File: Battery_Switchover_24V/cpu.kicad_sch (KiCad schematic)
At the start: 39 parts, among them J1 USB_C_Receptacle_USB2.0_14P, M1 Fan, Q1 PZT2222AT1G, SW1 SW_Push, U14 OPA2197xD, U3 LPC11U14FBD48-201, Y1 12.000MHz

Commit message: adding BMS and changed topology
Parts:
- D3: footprint Diode_THT:D_5W_P10.16mm_Horizontal -> Diode_SMD:D_SMA_Handsoldering
- M1: footprint Connector_PinHeader_2.54mm:PinHeader_1x02_P2.54mm_Vertical -> TerminalBlock_Phoenix:TerminalBlock_Phoenix_PT-1,5-2-3.5-H_1x02_P3.50mm_Horizontal
- Y1: footprint Crystal:Crystal_SMD_HC49-SD -> Crystal:Crystal_SMD_TXC_7M-4Pin_3.2x2.5mm
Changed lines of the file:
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@@
 			)
 		)
-		(property "Footprint" "Diode_THT:D_5W_P10.16mm_Horizontal"
+		(property "Footprint" "Diode_SMD:D_SMA_Handsoldering"
 			(at 248.92 120.65 0)
 			(effects
@@
 			)
 		)
-		(property "Footprint" "Crystal:Crystal_SMD_HC49-SD"
+		(property "Footprint" "Crystal:Crystal_SMD_TXC_7M-4Pin_3.2x2.5mm"
 			(at 148.59 107.95 0)
 			(effects
@@
 			)
 		)
-		(property "Footprint" "Connector_PinHeader_2.54mm:PinHeader_1x02_P2.54mm_Vertical"
+		(property "Footprint" "TerminalBlock_Phoenix:TerminalBlock_Phoenix_PT-1,5-2-3.5-H_1x02_P3.50mm_Horizontal"
 			(at 256.54 121.666 0)
 			(effects

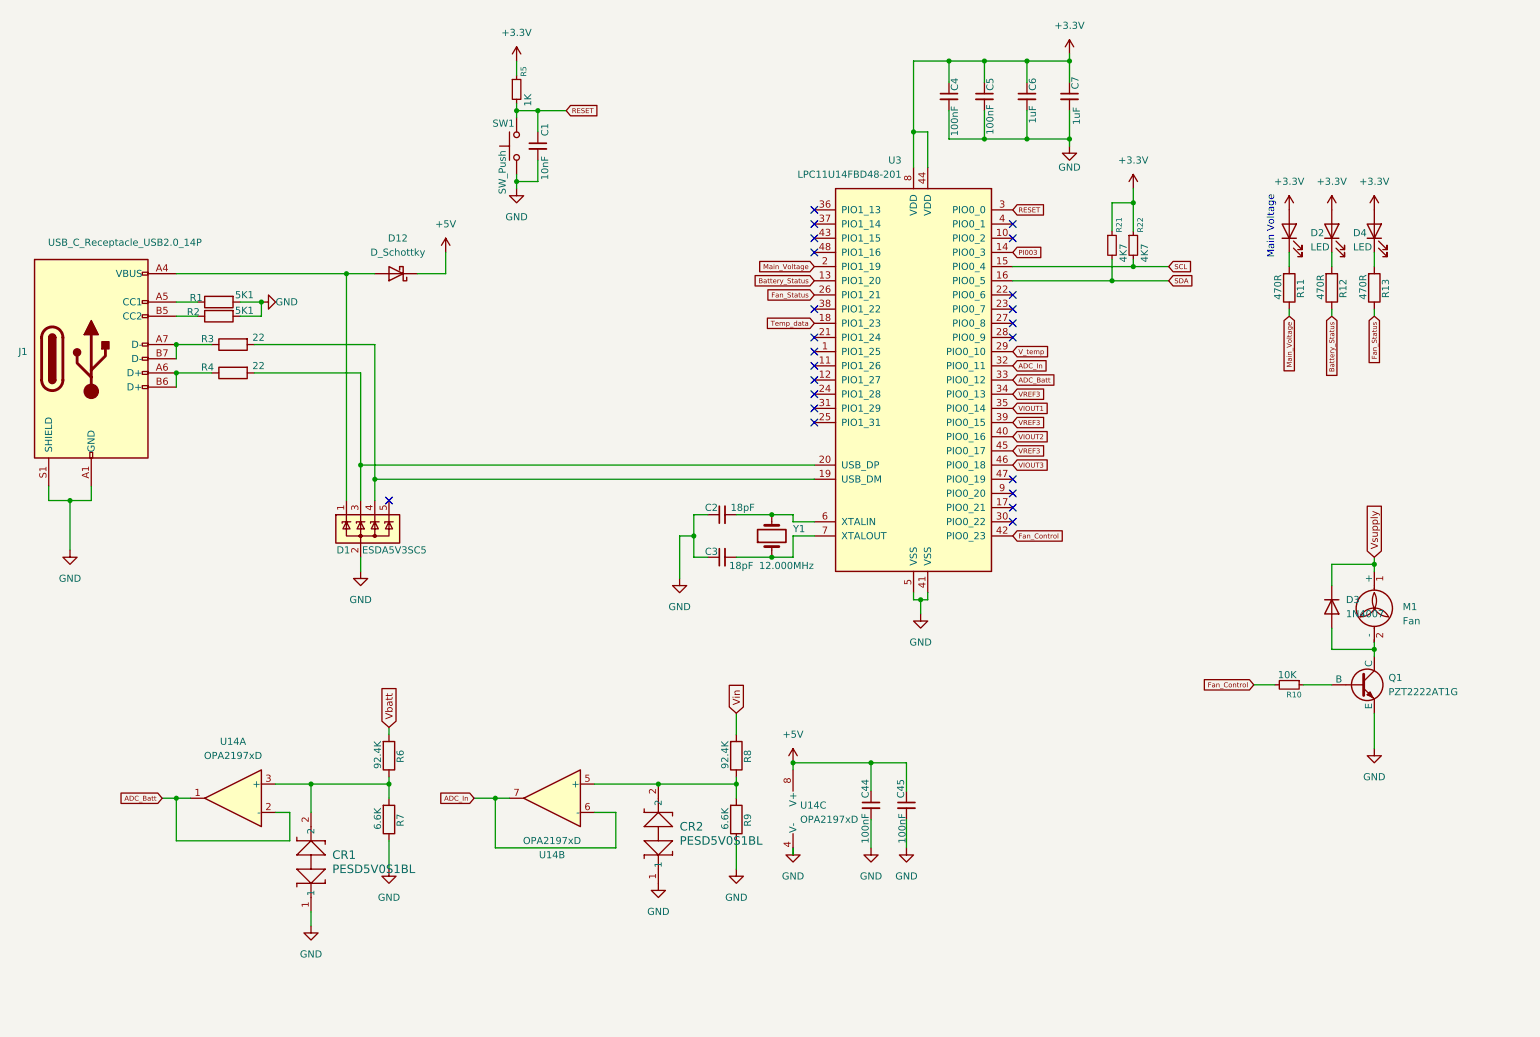
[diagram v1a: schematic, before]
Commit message: Changed current sensor (fewer analog pins), added extra adc
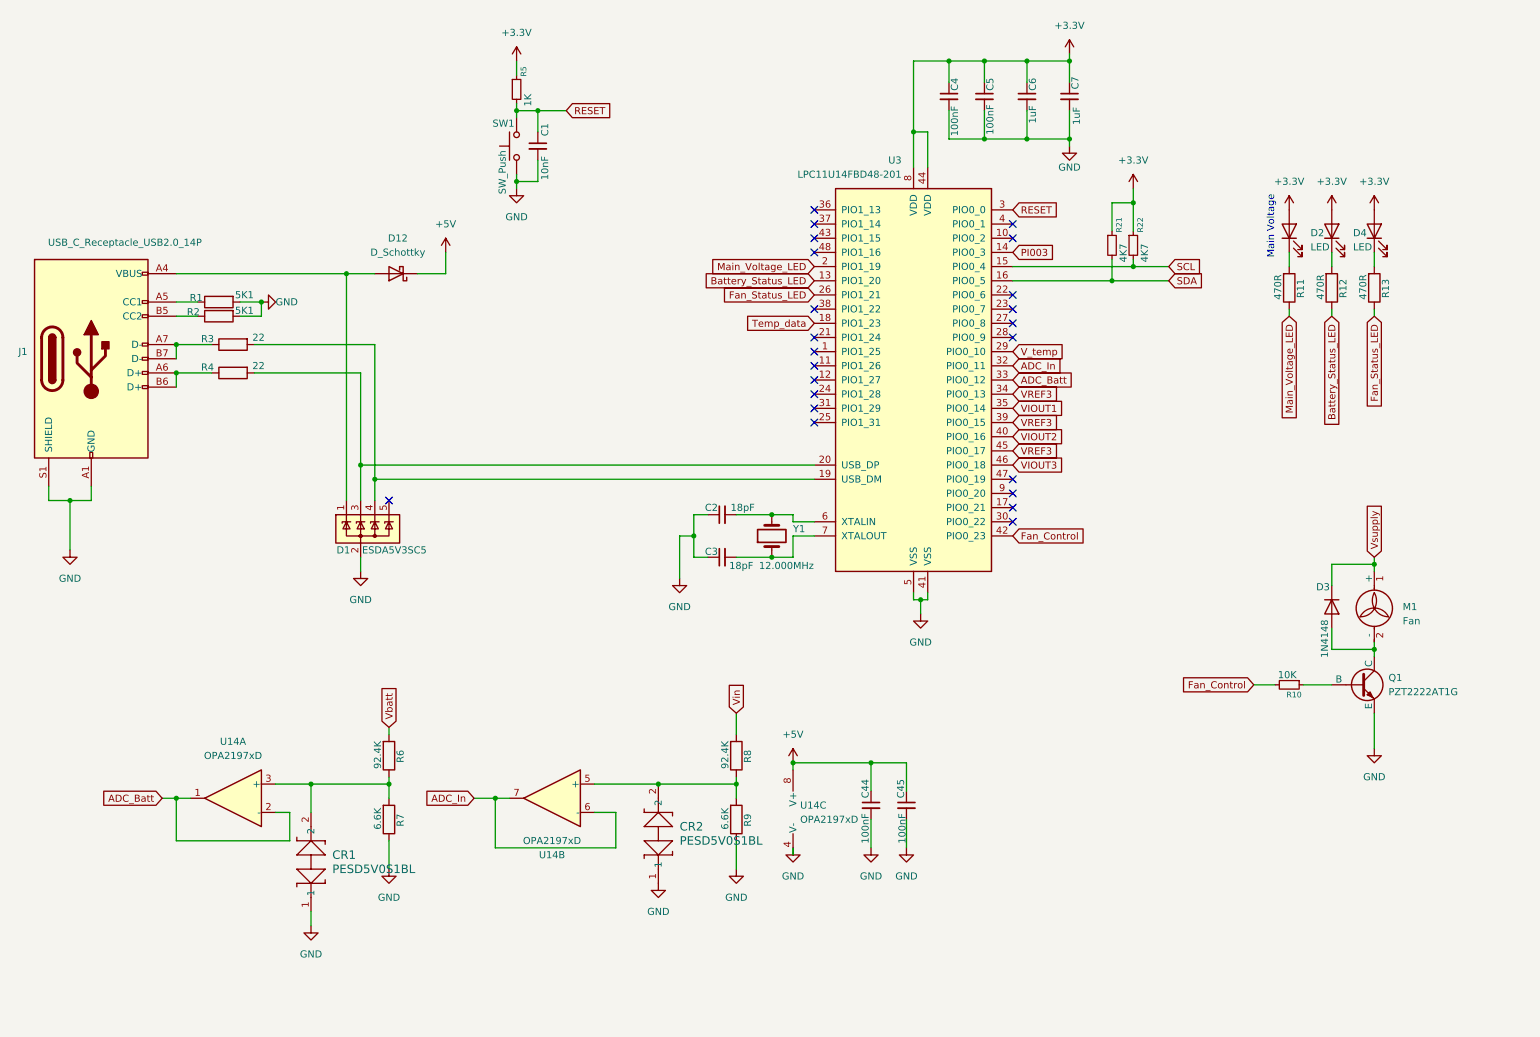
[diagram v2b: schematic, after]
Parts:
- D3: value 1N4007 -> 1N4148
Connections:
- net Battery_Status renamed Battery_Status_LED
- net Fan_Status renamed Fan_Status_LED
- net Main_Voltage renamed Main_Voltage_LED
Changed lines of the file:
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@@
 		)
 	)
-	(global_label "Fan_Status"
+	(global_label "Fan_Status_LED"
 		(shape input)
 		(at 156.21 64.77 180)
@@
 		(effects
 			(font
-				(size 0.889 0.889)
+				(size 1.27 1.27)
 			)
 			(justify right)
 		)
 		(property "Intersheetrefs" "${INTERSHEET_REFS}"
-			(at 146.8816 64.77 0)
+			(at 138.4689 64.77 0)
 			(effects
 				(font
@@
 		(effects
 			(font
-				(size 0.889 0.889)
+				(size 1.27 1.27)
 			)
 			(justify left)
@@
 		)
 	)
-	(global_label "Main_Voltage"
+	(global_label "Main_Voltage_LED"
 		(shape input)
 		(at 156.21 59.69 180)
@@
 		(effects
 			(font
-				(size 0.889 0.889)
+				(size 1.27 1.27)
 			)
 			(justify right)
 		)
 		(property "Intersheetrefs" "${INTERSHEET_REFS}"
-			(at 145.4847 59.69 0)
+			(at 136.4732 59.69 0)
 			(effects
 				(font
@@
 		(effects
 			(font
-				(size 0.889 0.889)
+				(size 1.27 1.27)
 			)
 			(justify left)
@@
 		)
 	)
-	(global_label "Battery_Status"
+	(global_label "Battery_Status_LED"
 		(shape input)
 		(at 156.21 62.23 180)
@@
 		(effects
 			(font
-				(size 0.889 0.889)
+				(size 1.27 1.27)
 			)
 			(justify right)
 		)
 		(property "Intersheetrefs" "${INTERSHEET_REFS}"
-			(at 144.5533 62.23 0)
+			(at 135.1427 62.23 0)
 			(effects
 				(font
@@
 		(effects
 			(font
-				(size 0.889 0.889)
-			)
-			(justify left)
-		)
-		(property "Intersheetrefs" "${INTERSHEET_REFS}"
-			(at 197.8811 49.53 0)
+				(size 1.27 1.27)
+			)
+			(justify left)
+		)
+		(property "Intersheetrefs" "${INTERSHEET_REFS}"
+			(at 200.5003 49.53 0)
 			(effects
 				(font
@@
 		(effects
 			(font
-				(size 0.889 0.889)
-			)
-			(justify left)
-		)
-		(property "Intersheetrefs" "${INTERSHEET_REFS}"
-			(at 224.2972 62.23 0)
+				(size 1.27 1.27)
+			)
+			(justify left)
+		)
+		(property "Intersheetrefs" "${INTERSHEET_REFS}"
+			(at 226.2633 62.23 0)
 			(effects
 				(font
@@
 		(effects
 			(font
-				(size 0.889 0.889)
+				(size 1.27 1.27)
 			)
 			(justify left)
@@
 		(effects
 			(font
-				(size 0.889 0.889)
-			)
-			(justify left)
-		)
-		(property "Intersheetrefs" "${INTERSHEET_REFS}"
-			(at 224.2549 59.69 0)
+				(size 1.27 1.27)
+			)
+			(justify left)
+		)
+		(property "Intersheetrefs" "${INTERSHEET_REFS}"
+			(at 226.2028 59.69 0)
 			(effects
 				(font
@@
 		(effects
 			(font
-				(size 0.889 0.889)
+				(size 1.27 1.27)
 			)
 			(justify left)
@@
 		(effects
 			(font
-				(size 0.889 0.889)
+				(size 1.27 1.27)
 			)
 			(justify left)
@@
 		(effects
 			(font
-				(size 0.889 0.889)
+				(size 1.27 1.27)
 			)
 			(justify right)
@@
 		(effects
 			(font
-				(size 0.889 0.889)
+				(size 1.27 1.27)
 			)
 			(justify left)
@@
 		(effects
 			(font
-				(size 0.889 0.889)
+				(size 1.27 1.27)
 			)
 			(justify right)
@@
 		(effects
 			(font
-				(size 0.889 0.889)
-			)
-			(justify left)
-		)
-		(property "Intersheetrefs" "${INTERSHEET_REFS}"
-			(at 197.7119 57.15 0)
+				(size 1.27 1.27)
+			)
+			(justify left)
+		)
+		(property "Intersheetrefs" "${INTERSHEET_REFS}"
+			(at 200.2585 57.15 0)
 			(effects
 				(font
@@
 		(effects
 			(font
-				(size 0.889 0.889)
+				(size 1.27 1.27)
 			)
 			(justify right)
 		)
 		(property "Intersheetrefs" "${INTERSHEET_REFS}"
-			(at 147.0934 69.85 0)
+			(at 143.186 69.85 0)
 			(effects
 				(font
@@
 		(effects
 			(font
-				(size 0.889 0.889)
+				(size 1.27 1.27)
 			)
 			(justify left)
@@
 		)
 	)
-	(global_label "Main_Voltage"
+	(global_label "Main_Voltage_LED"
 		(shape input)
 		(at 241.3 68.58 270)
@@
 		(effects
 			(font
-				(size 0.889 0.889)
+				(size 1.27 1.27)
 			)
 			(justify right)
 		)
 		(property "Intersheetrefs" "${INTERSHEET_REFS}"
-			(at 241.3 79.3053 90)
+			(at 241.3 82.3956 90)
 			(effects
 				(font
@@
 		)
 	)
-	(global_label "Battery_Status"
+	(global_label "Battery_Status_LED"
 		(shape input)
 		(at 248.92 68.58 270)
@@
 		(effects
 			(font
-				(size 0.889 0.889)
+				(size 1.27 1.27)
 			)
 			(justify right)
 		)
 		(property "Intersheetrefs" "${INTERSHEET_REFS}"
-			(at 248.92 80.2367 90)
+			(at 248.92 83.327 90)
 			(effects
 				(font
@@
 		(effects
 			(font
-				(size 0.889 0.889)
+				(size 1.27 1.27)
 			)
 			(justify left)
@@
 		)
 	)
-	(global_label "Fan_Status"
+	(global_label "Fan_Status_LED"
 		(shape input)
 		(at 256.54 68.58 270)
@@
 		(effects
 			(font
-				(size 0.889 0.889)
+				(size 1.27 1.27)
 			)
 			(justify right)
 		)
 		(property "Intersheetrefs" "${INTERSHEET_REFS}"
-			(at 256.54 77.9084 90)
+			(at 256.54 80.9987 90)
 			(effects
 				(font
@@
 		(effects
 			(font
-				(size 0.889 0.889)
+				(size 1.27 1.27)
 			)
 			(justify right)
@@
 		(effects
 			(font
-				(size 0.889 0.889)
+				(size 1.27 1.27)
 			)
 			(justify left)
@@
 		(effects
 			(font
-				(size 0.889 0.889)
+				(size 1.27 1.27)
 			)
 			(justify left)
@@
 		(effects
 			(font
-				(size 0.889 0.889)
+				(size 1.27 1.27)
 			)
 			(justify left)
@@
 		(on_board yes)
 		(dnp no)
-		(fields_autoplaced yes)
 		(property "Reference" "D3"
-			(at 251.46 119.3799 90)
-			(effects
-				(font
-					(size 1.27 1.27)
-				)
-				(justify left)
-			)
-		)
-		(property "Value" "1N4007"
-			(at 251.46 121.9199 90)
-			(effects
-				(font
+			(at 246.126 117.094 90)
+			(effects
+				(font
+					(size 1.27 1.27)
+				)
+				(justify left)
+			)
+		)
+		(property "Value" "1N4148"
+			(at 247.65 122.936 0)
+			(effects
+				(font

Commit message: Labels assigned
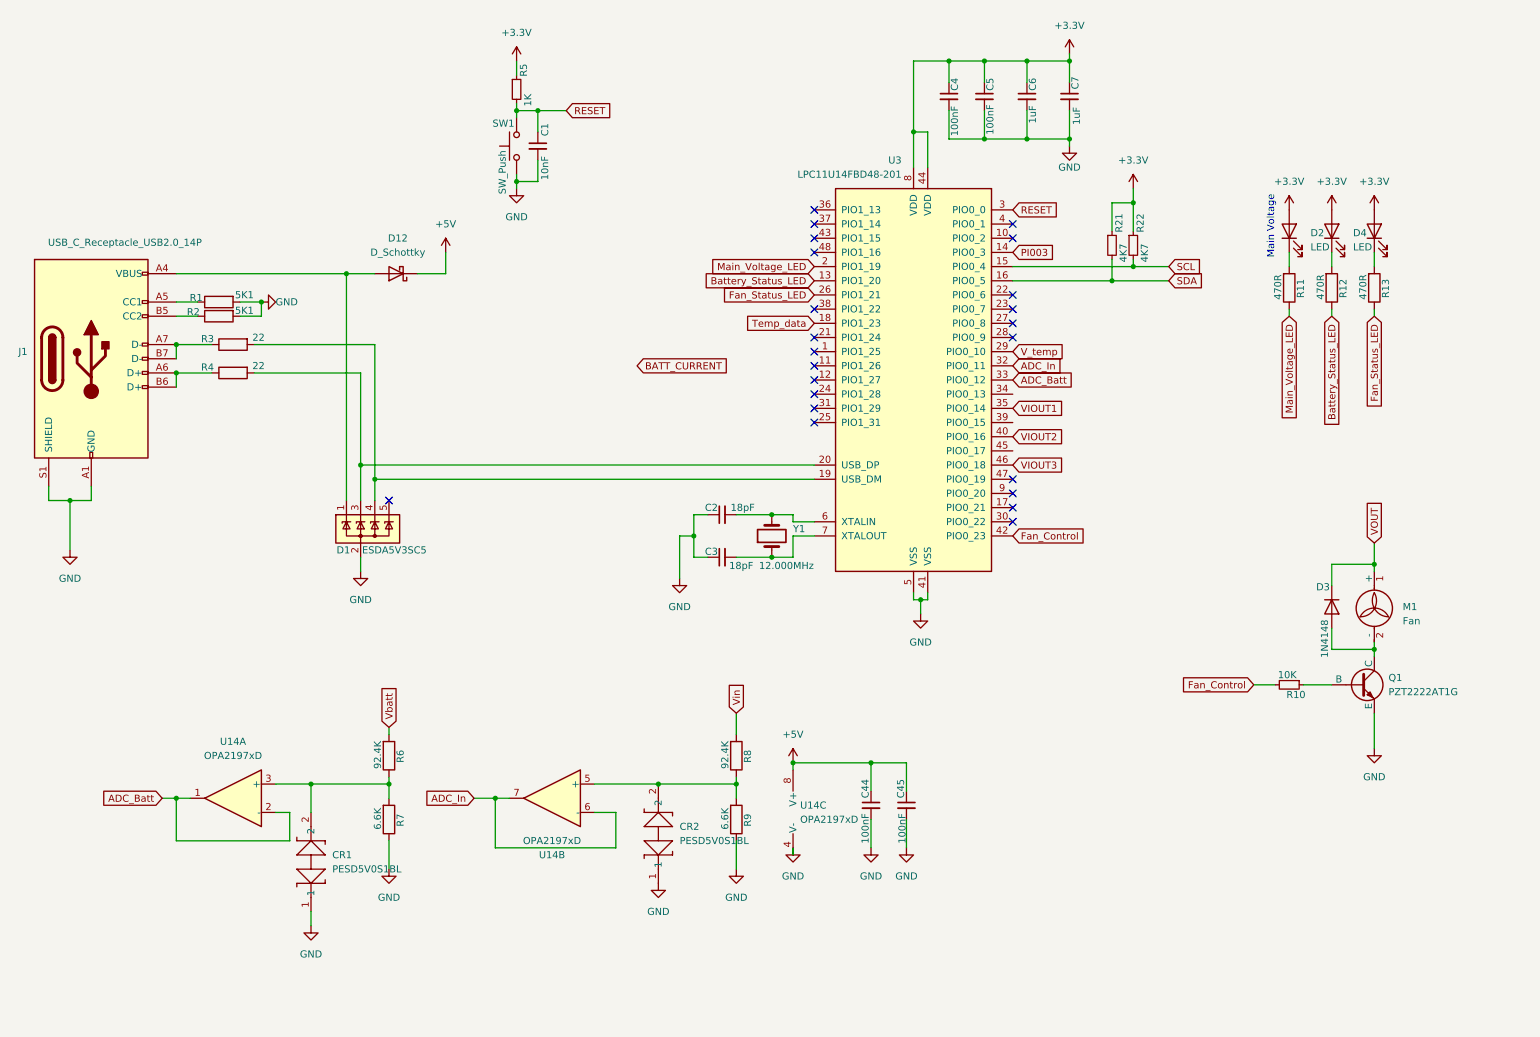
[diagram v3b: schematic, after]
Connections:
- removed net VREF3: U3.34 (PIO0_13), U3.39 (PIO0_15), U3.45 (PIO0_17)
- net Vsupply renamed VOUT
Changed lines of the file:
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@@
 	(wire
 		(pts
+			(xy 256.54 109.22) (xy 256.54 113.03)
+		)
+		(stroke
+			(width 0)
+			(type default)
+		)
+	)
+	(wire
+		(pts
 			(xy 22.86 101.6) (xy 22.86 110.49)
 		)
@@
 	(wire
 		(pts
-			(xy 256.54 111.76) (xy 256.54 113.03)
-		)
-		(stroke
-			(width 0)
-			(type default)
-		)
-	)
-	(wire
-		(pts
 			(xy 39.37 154.94) (xy 41.91 154.94)
 		)
@@
 		)
 	)
-	(global_label "VREF3"
+	(global_label "VOUT"
 		(shape input)
-		(at 191.77 87.63 0)
+		(at 256.54 109.22 90)
 		(fields_autoplaced yes)
 		(effects
@@
 		)
 		(property "Intersheetrefs" "${INTERSHEET_REFS}"
-			(at 197.9235 87.63 0)
+			(at 256.54 101.5176 90)
 			(effects
 				(font
@@
 		)
 	)
-	(global_label "VREF3"
+	(global_label "BATT_CURRENT"
 		(shape input)
-		(at 191.77 82.55 0)
+		(at 124.46 77.47 0)
 		(fields_autoplaced yes)
 		(effects
@@
 		)
 		(property "Intersheetrefs" "${INTERSHEET_REFS}"
-			(at 197.9235 82.55 0)
+			(at 141.2942 77.47 0)
 			(effects
 				(font
@@
 		)
 	)
-	(global_label "VREF3"
-		(shape input)
-		(at 191.77 92.71 0)
-		(fields_autoplaced yes)
-		(effects
-			(font
-				(size 1.27 1.27)
-			)
-			(justify left)
-		)
-		(property "Intersheetrefs" "${INTERSHEET_REFS}"
-			(at 197.9235 92.71 0)
-			(effects
-				(font
-					(size 1.27 1.27)
-				)
-				(justify left)
-				(hide yes)
-			)
-		)
-	)
 	(global_label "Main_Voltage_LED"
 		(shape input)
@@
 		)
 	)
-	(global_label "Vsupply"
-		(shape input)
-		(at 256.54 111.76 90)
-		(fields_autoplaced yes)
-		(effects
-			(font
-				(size 1.27 1.27)
-			)
-			(justify left)
-		)
-		(property "Intersheetrefs" "${INTERSHEET_REFS}"
-			(at 256.54 101.5783 90)
-			(effects
-				(font
-					(size 1.27 1.27)
-				)
-				(justify left)
-				(hide yes)
-			)
-		)
-	)
 	(global_label "Fan_Control"
 		(shape input)
@@
 			(effects
 				(font
-					(size 1.016 1.016)
+					(size 1.27 1.27)
 				)
 				(justify left)
@@
 			(effects
 				(font
-					(size 1.524 1.524)
+					(size 1.27 1.27)
 				)
 				(justify right)
@@
 			(effects
 				(font
-					(size 1.524 1.524)
+					(size 1.27 1.27)
 				)
 				(justify right)
@@
 			(effects
 				(font
-					(size 1.016 1.016)
+					(size 1.27 1.27)
 				)
 				(justify left)
@@
 			(effects
 				(font
-					(size 1.016 1.016)
+					(size 1.27 1.27)
 				)
 				(justify left)
@@
 			(effects
 				(font
-					(size 1.524 1.524)
+					(size 1.27 1.27)
 				)
 				(justify right)
@@
 			(effects
 				(font
-					(size 1.524 1.524)
+					(size 1.27 1.27)
 				)
 				(justify right)
@@
 			(effects
 				(font
-					(size 1.016 1.016)
+					(size 1.27 1.27)
 				)
 				(justify left)
